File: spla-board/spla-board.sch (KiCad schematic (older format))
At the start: 25 parts

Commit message: schematic: Add some notes.
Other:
- note added: "How do I move this symbol name inside the box?"
- note added: "Not sure how to hook up AD/AC/BD/BC buses yet."
- note added: "What is this inductor for?\nJust LC filtering input power?"
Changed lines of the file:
@@
 Text Notes 7200 1950 0    50   ~ 0
 Decoupling Capacitors\n
+Text Notes 11550 5550 0    50   ~ 0
+Not sure how to hook up AD/AC/BD/BC buses yet.
+Text Notes 9850 3100 0    25   ~ 0
+How do I move this symbol name inside the box?
+Text Notes 2100 9000 0    25   ~ 0
+What is this inductor for?\nJust LC filtering input power?
 $EndSCHEMATC

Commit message: schematic: Swap R_US for R.
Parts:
- R? (x8): symbol Device:R_US -> Device:R
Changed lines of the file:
@@
 $EndComp
 $Comp
-L Device:R_US R?
+L Device:R R?
 U 1 1 5E4AB80E
 P 2400 9850
@@
 Wire Wire Line
 	3500 8500 3650 8500
-$Comp
-L Device:R_US R?
-U 1 1 5E4DC0A0
-P 3350 8500
-F 0 "R?" V 3145 8500 50  0000 C CNN
-F 1 "1K" V 3236 8500 50  0000 C CNN
-F 2 "" V 3390 8490 50  0001 C CNN
-F 3 "~" H 3350 8500 50  0001 C CNN
-	1    3350 8500
-	0    1    1    0
-$EndComp
 Wire Wire Line
 	3650 8500 3650 8650
@@
 	7250 5950 7250 6350
 $Comp
-L Device:R_US R?
+L Device:R R?
 U 1 1 5E55BD51
 P 6800 6850
@@
 	8750 4850 8250 4850
 $Comp
-L Device:R_US R?
+L Device:R R?
 U 1 1 5E571C78
 P 6400 5600
@@
 $EndComp
 $Comp
-L Device:R_US R?
+L Device:R R?
 U 1 1 5E572548
 P 6850 5600
@@
 $EndComp
 $Comp
-L Device:R_US R?
+L Device:R R?
 U 1 1 5E572B74
 P 7250 5600
@@
 Connection ~ 1550 6350
 $Comp
-L Device:R_US R?
+L Device:R R?
 U 1 1 5E60E8AF
 P 8200 5250
@@
 	8200 5050 8200 5100
 $Comp
-L Device:R_US R?
+L Device:R R?
 U 1 1 5E619C52
 P 8700 5600
@@
 Text Notes 2100 9000 0    25   ~ 0
 What is this inductor for?\nJust LC filtering input power?
+$Comp
+L Device:R R?
+U 1 1 5E4DC0A0
+P 3350 8500
+F 0 "R?" V 3145 8500 50  0000 C CNN
+F 1 "1K" V 3236 8500 50  0000 C CNN
+F 2 "" V 3390 8490 50  0001 C CNN
+F 3 "~" H 3350 8500 50  0001 C CNN
+	1    3350 8500
+	0    1    1    0
+$EndComp
 $EndSCHEMATC

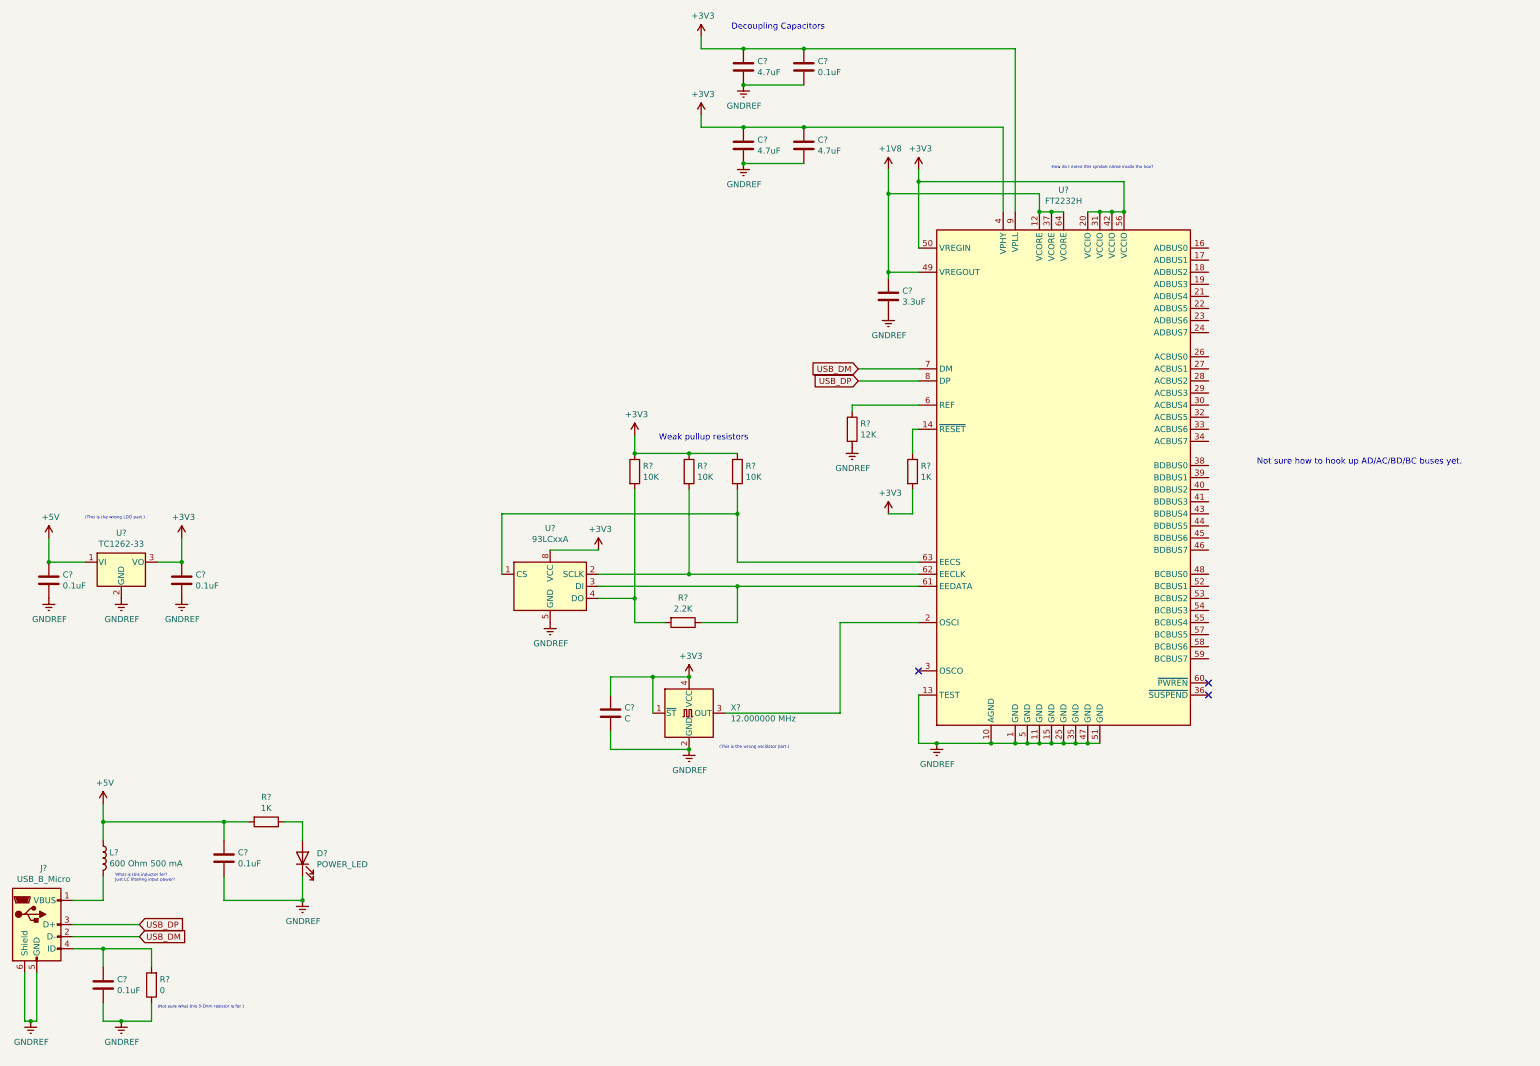
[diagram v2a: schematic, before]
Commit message: schematic: Swap GNDREF for GND.
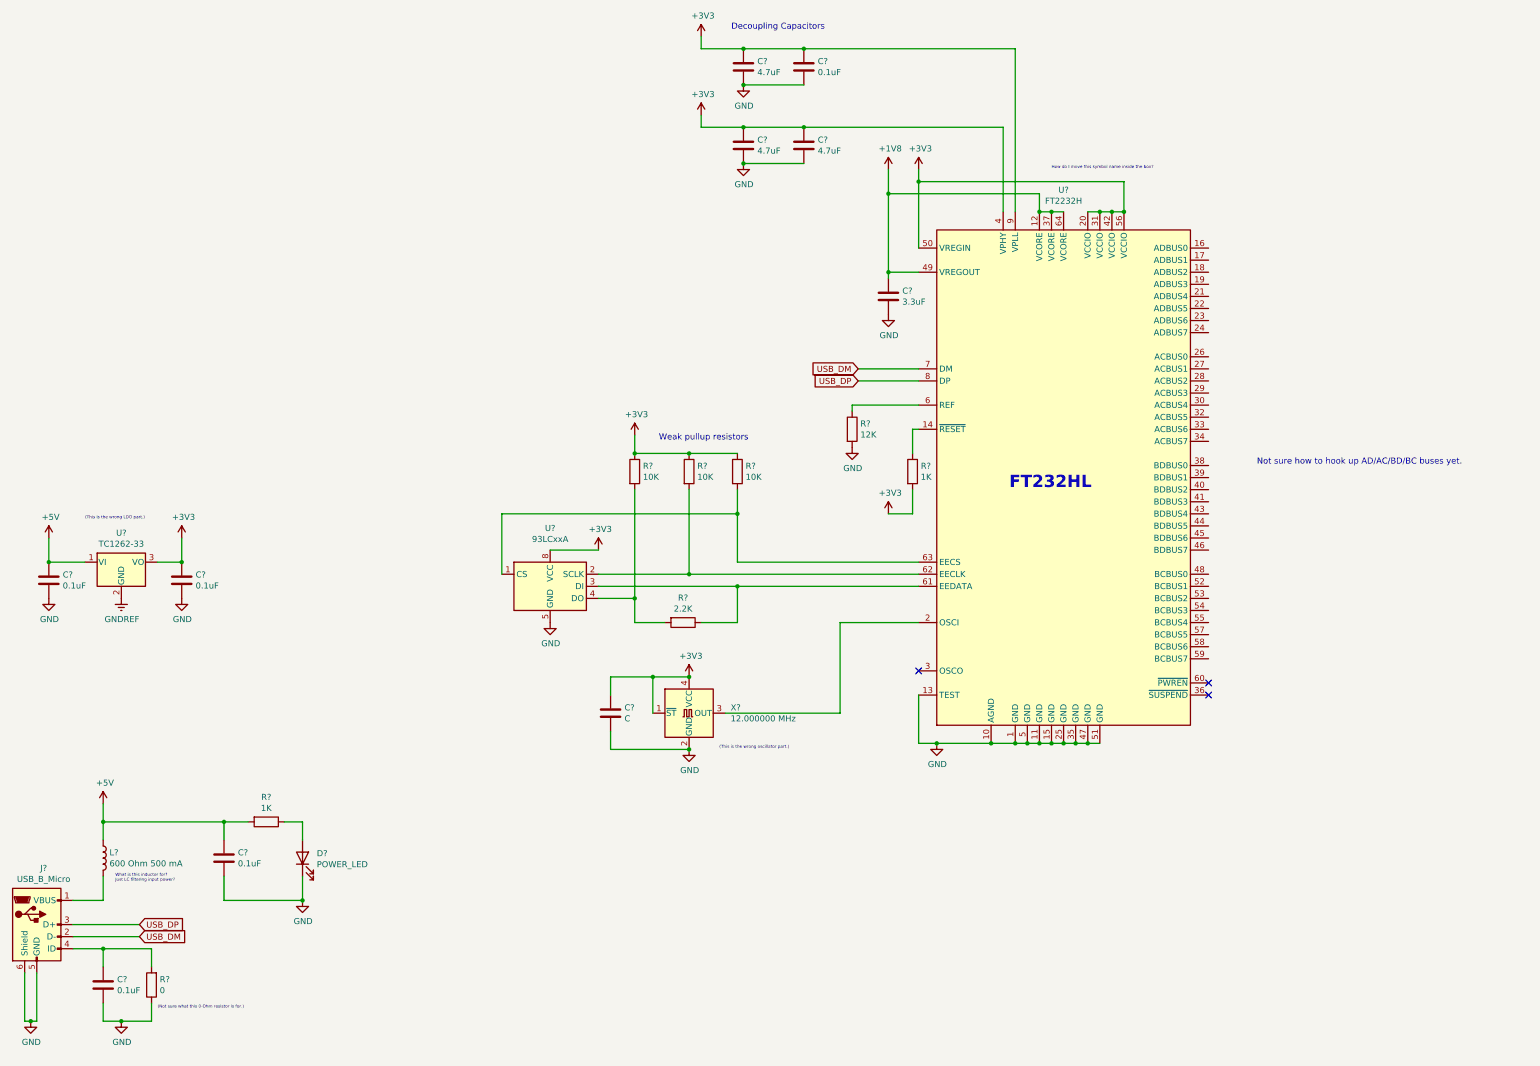
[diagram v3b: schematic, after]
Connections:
- net GNDREF: no longer C?.1, C?.1, C?.2, C?.2, C?.2, C?.2, C?.2, C?.2, C?.2, C?.2, D?.1 (K), J?.5 (GND), J?.6 (Shield), R?.1, R?.2, U?.1 (GND), U?.10 (AGND), U?.11 (GND), U?.13 (TEST), U?.15 (GND), U?.25 (GND), U?.35 (GND), U?.47 (GND), U?.5 (GND), U?.5 (GND), U?.51 (GND), X?.2 (GND)
- new net GND: C?.1, C?.1, C?.2, C?.2, C?.2, C?.2, C?.2, C?.2, C?.2, C?.2, D?.1 (K), J?.5 (GND), J?.6 (Shield), R?.1, R?.2, U?.1 (GND), U?.10 (AGND), U?.11 (GND), U?.13 (TEST), U?.15 (GND), U?.25 (GND), U?.35 (GND), U?.47 (GND), U?.5 (GND), U?.5 (GND), U?.51 (GND), X?.2 (GND)
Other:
- note added: "FT232HL"
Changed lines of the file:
@@
 	1750 9450 2300 9450
 $Comp
-L power:GNDREF #PWR0101
+L power:GND #PWR0101
 U 1 1 5E4AD97D
 P 1400 10150
 F 0 "#PWR0101" H 1400 9900 50  0001 C CNN
-F 1 "GNDREF" H 1405 9977 50  0000 C CNN
+F 1 "GND" H 1405 9977 50  0000 C CNN
 F 2 "" H 1400 10150 50  0001 C CNN
 F 3 "" H 1400 10150 50  0001 C CNN
@@
 	2400 10000 2400 10150
 $Comp
-L power:GNDREF #PWR0102
+L power:GND #PWR0102
 U 1 1 5E4C66E6
 P 2150 10150
 F 0 "#PWR0102" H 2150 9900 50  0001 C CNN
-F 1 "GNDREF" H 2155 9977 50  0000 C CNN
+F 1 "GND" H 2155 9977 50  0000 C CNN
 F 2 "" H 2150 10150 50  0001 C CNN
 F 3 "" H 2150 10150 50  0001 C CNN
@@
 $EndComp
 $Comp
-L power:GNDREF #PWR0103
+L power:GND #PWR0103
 U 1 1 5E4E0513
 P 3650 9150
 F 0 "#PWR0103" H 3650 8900 50  0001 C CNN
-F 1 "GNDREF" H 3655 8977 50  0000 C CNN
+F 1 "GND" H 3655 8977 50  0000 C CNN
 F 2 "" H 3650 9150 50  0001 C CNN
 F 3 "" H 3650 9150 50  0001 C CNN
@@
 $EndComp
 $Comp
-L power:GNDREF #PWR0105
+L power:GND #PWR0105
 U 1 1 5E52FAA0
 P 8900 7850
 F 0 "#PWR0105" H 8900 7600 50  0001 C CNN
-F 1 "GNDREF" H 8905 7677 50  0000 C CNN
+F 1 "GND" H 8905 7677 50  0000 C CNN
 F 2 "" H 8900 7850 50  0001 C CNN
 F 3 "" H 8900 7850 50  0001 C CNN
@@
 	6550 7300 6200 7300
 $Comp
-L power:GNDREF #PWR0106
+L power:GND #PWR0106
 U 1 1 5E558255
 P 5700 6850
 F 0 "#PWR0106" H 5700 6600 50  0001 C CNN
-F 1 "GNDREF" H 5705 6677 50  0000 C CNN
+F 1 "GND" H 5705 6677 50  0000 C CNN
 F 2 "" H 5700 6850 50  0001 C CNN
 F 3 "" H 5700 6850 50  0001 C CNN
@@
 Connection ~ 7250 5950
 $Comp
-L power:GNDREF #PWR0108
+L power:GND #PWR0108
 U 1 1 5E58FEB5
 P 6850 7900
 F 0 "#PWR0108" H 6850 7650 50  0001 C CNN
-F 1 "GNDREF" H 6855 7727 50  0000 C CNN
+F 1 "GND" H 6855 7727 50  0000 C CNN
 F 2 "" H 6850 7900 50  0001 C CNN
 F 3 "" H 6850 7900 50  0001 C CNN
@@
 $EndComp
 $Comp
-L power:GNDREF #PWR?
+L power:GND #PWR?
 U 1 1 5E5E7F66
 P 8500 4300
 F 0 "#PWR?" H 8500 4050 50  0001 C CNN
-F 1 "GNDREF" H 8505 4127 50  0000 C CNN
+F 1 "GND" H 8505 4127 50  0000 C CNN
 F 2 "" H 8500 4300 50  0001 C CNN
 F 3 "" H 8500 4300 50  0001 C CNN
@@
 Connection ~ 2650 6350
 $Comp
-L power:GNDREF #PWR?
+L power:GND #PWR?
 U 1 1 5E5FD67A
 P 2650 6650
 F 0 "#PWR?" H 2650 6400 50  0001 C CNN
-F 1 "GNDREF" H 2655 6477 50  0000 C CNN
+F 1 "GND" H 2655 6477 50  0000 C CNN
 F 2 "" H 2650 6650 50  0001 C CNN
 F 3 "" H 2650 6650 50  0001 C CNN
@@
 $EndComp
 $Comp
-L power:GNDREF #PWR?
+L power:GND #PWR?
 U 1 1 5E603CC8
 P 1550 6650
 F 0 "#PWR?" H 1550 6400 50  0001 C CNN
-F 1 "GNDREF" H 1555 6477 50  0000 C CNN
+F 1 "GND" H 1555 6477 50  0000 C CNN
 F 2 "" H 1550 6650 50  0001 C CNN
 F 3 "" H 1550 6650 50  0001 C CNN
@@
 $EndComp
 $Comp
-L power:GNDREF #PWR?
+L power:GND #PWR?
 U 1 1 5E616CF7
 P 8200 5400
 F 0 "#PWR?" H 8200 5150 50  0001 C CNN
-F 1 "GNDREF" H 8205 5227 50  0000 C CNN
+F 1 "GND" H 8205 5227 50  0000 C CNN
 F 2 "" H 8200 5400 50  0001 C CNN
 F 3 "" H 8200 5400 50  0001 C CNN
@@
 	9550 2100 9550 3450
 $Comp
-L power:GNDREF #PWR?
+L power:GND #PWR?
 U 1 1 5E6F4907
 P 7300 2400
 F 0 "#PWR?" H 7300 2150 50  0001 C CNN
-F 1 "GNDREF" H 7305 2227 50  0000 C CNN
+F 1 "GND" H 7305 2227 50  0000 C CNN
 F 2 "" H 7300 2400 50  0001 C CNN
 F 3 "" H 7300 2400 50  0001 C CNN
@@
 $EndComp
 $Comp
-L power:GNDREF #PWR?
+L power:GND #PWR?
 U 1 1 5E6F5039
 P 7300 3050
 F 0 "#PWR?" H 7300 2800 50  0001 C CNN
-F 1 "GNDREF" H 7305 2877 50  0000 C CNN
+F 1 "GND" H 7305 2877 50  0000 C CNN
 F 2 "" H 7300 3050 50  0001 C CNN
 F 3 "" H 7300 3050 50  0001 C CNN
@@
 	0    1    1    0
 $EndComp
+Text Notes 9500 5750 0    101  ~ 20
+FT232HL
 $EndSCHEMATC

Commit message: schematic: Add root schematic sheet.
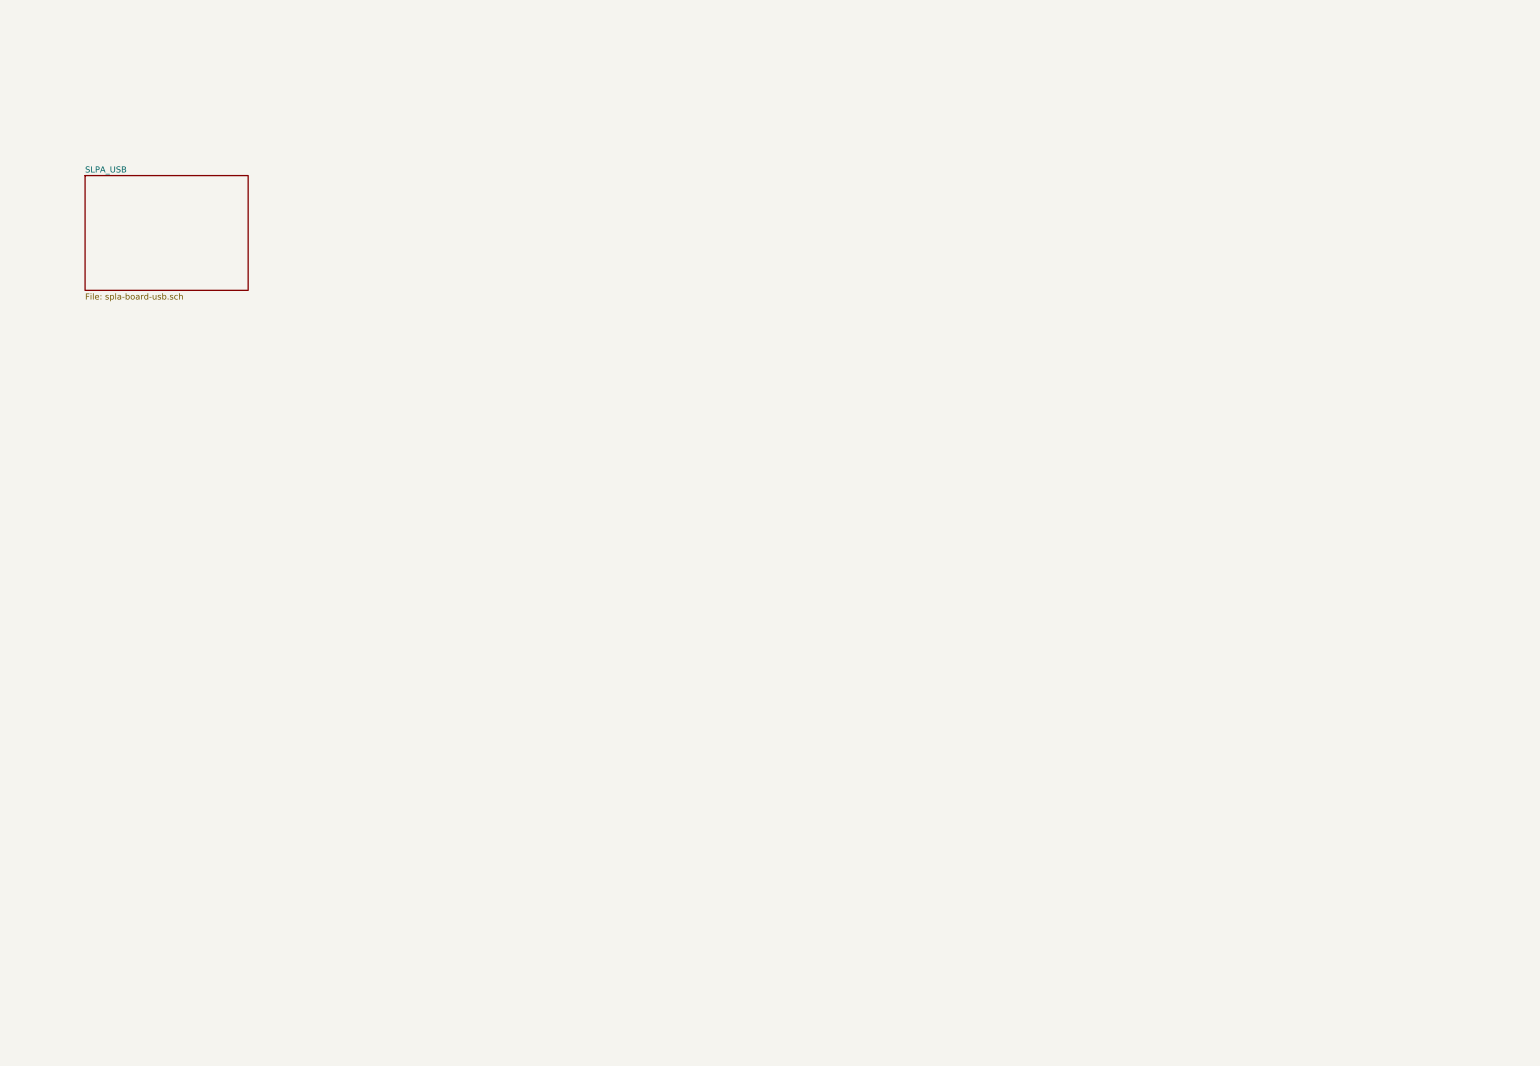
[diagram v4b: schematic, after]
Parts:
- removed C? (x5): 0.1uF, symbol Device:C
- removed C?: C, symbol Device:C
- removed C?: 3.3uF, symbol Device:C
- removed C? (x3): 4.7uF, symbol Device:C
- removed D?: POWER_LED, symbol Device:LED
- removed J?: USB_B_Micro, symbol Connector:USB_B_Micro
- removed L?: 600 Ohm 500 mA, symbol Device:L
- removed R?: 0, symbol Device:R
- removed R? (x2): 1K, symbol Device:R
- removed R?: 2.2K, symbol Device:R
- removed R? (x3): 10K, symbol Device:R
- removed R?: 12K, symbol Device:R
- removed U?: FT2232H, symbol Interface_USB:FT2232H
- removed U?: 93LCxxA, symbol Memory_EEPROM:93LCxxA
- removed U?: TC1262-33, symbol Regulator_Linear:TC1262-33
- removed X?: 12.000000 MHz, Oscillator:Oscillator_SMD_SeikoEpson_SG8002LB-4Pin_5.0x3.2mm, symbol Oscillator:SG-5032CAN
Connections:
- no-connect marks 3 -> 0
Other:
- note removed: "(Not sure what this 0-Ohm resistor is for.)"
- note removed: "(This is the wrong LDO part.)"
- note removed: "(This is the wrong oscillator part.)"
- note removed: "Decoupling Capacitors\n"
- note removed: "FT232HL"
- note removed: "How do I move this symbol name inside the box?"
- note removed: "Not sure how to hook up AD/AC/BD/BC buses yet."
- note removed: "Weak pullup resistors"
- note removed: "What is this inductor for?\nJust LC filtering input power?"
